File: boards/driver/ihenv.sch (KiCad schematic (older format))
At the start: 8 parts, among them Q63 MMBT2222, Q64 MMBT2907, Q65 MMBT2222

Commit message: Driver board: a bit more schematic work and some initial footprint selections
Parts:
- R175, R176, R177, R178, R179: footprint Resistor_SMD:R_1206_3216Metric -> Resistor_SMD:R_0603_1608Metric
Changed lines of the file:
@@
 F 0 "R170" V 3745 3650 50  0000 C CNN
 F 1 "1k" V 3836 3650 50  0000 C CNN
-F 2 "Resistor_SMD:R_1206_3216Metric" V 3990 3640 50  0001 C CNN
+F 2 "Resistor_SMD:R_0603_1608Metric" V 3990 3640 50  0001 C CNN
 F 3 "~" H 3950 3650 50  0001 C CNN
 	1    3950 3650
@@
 F 0 "R172" H 4568 3296 50  0000 L CNN
 F 1 "2k" H 4568 3205 50  0000 L CNN
-F 2 "Resistor_SMD:R_1206_3216Metric" V 4540 3240 50  0001 C CNN
+F 2 "Resistor_SMD:R_0603_1608Metric" V 4540 3240 50  0001 C CNN
 F 3 "~" H 4500 3250 50  0001 C CNN
 	1    4500 3250
@@
 F 0 "R171" H 4568 2896 50  0000 L CNN
 F 1 "470" H 4568 2805 50  0000 L CNN
-F 2 "Resistor_SMD:R_1206_3216Metric" V 4540 2840 50  0001 C CNN
+F 2 "Resistor_SMD:R_0603_1608Metric" V 4540 2840 50  0001 C CNN
 F 3 "~" H 4500 2850 50  0001 C CNN
 	1    4500 2850
@@
 F 0 "R173" H 5168 3746 50  0000 L CNN
 F 1 "750" H 5168 3655 50  0000 L CNN
-F 2 "Resistor_SMD:R_1206_3216Metric" V 5140 3690 50  0001 C CNN
+F 2 "Resistor_SMD:R_0603_1608Metric" V 5140 3690 50  0001 C CNN
 F 3 "~" H 5100 3700 50  0001 C CNN
 	1    5100 3700
@@
 F 0 "R174" H 5718 3946 50  0000 L CNN
 F 1 "2k" H 5718 3855 50  0000 L CNN
-F 2 "Resistor_SMD:R_1206_3216Metric" V 5690 3890 50  0001 C CNN
+F 2 "Resistor_SMD:R_0603_1608Metric" V 5690 3890 50  0001 C CNN
 F 3 "~" H 5650 3900 50  0001 C CNN
 	1    5650 3900

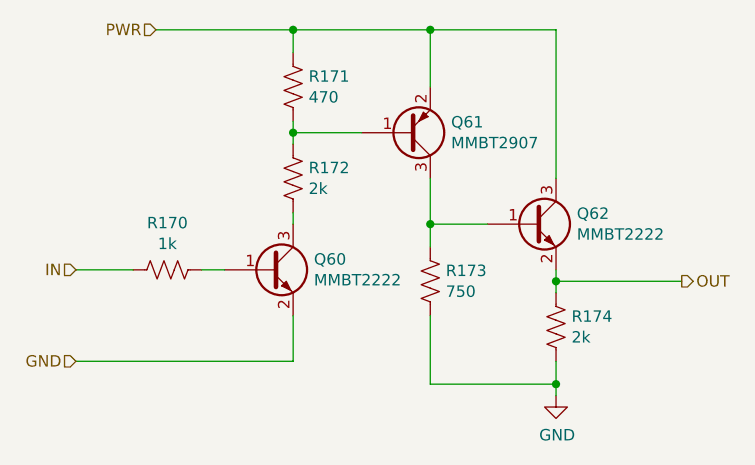
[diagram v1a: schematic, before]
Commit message: Driver board: finished first rough draft schematic. Lots of placeholders, but at least every place is held.
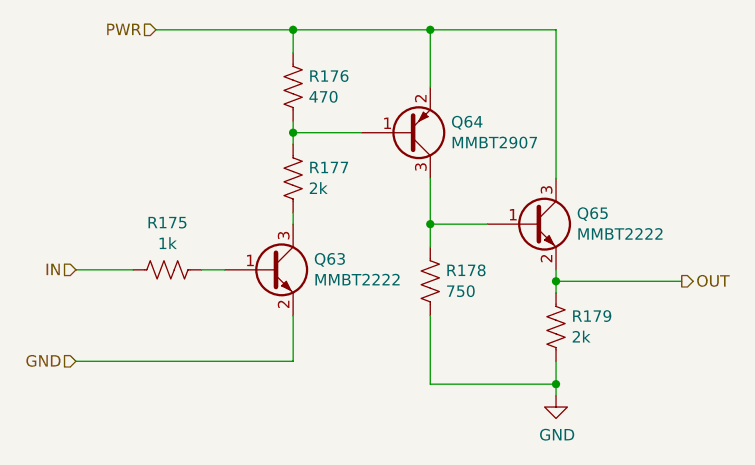
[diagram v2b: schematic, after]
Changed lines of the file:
@@
 $Descr A4 11693 8268
 encoding utf-8
-Sheet 48 68
+Sheet 48 69
 Title ""
 Date ""
@@
 AR Path="/6183FAE6/62401C49/62406F41" Ref="R175"  Part="1"
 AR Path="/6183FAE6/62435917/62406F41" Ref="R170"  Part="1"
-F 0 "R170" V 3745 3650 50  0000 C CNN
+F 0 "R175" V 3745 3650 50  0000 C CNN
 F 1 "1k" V 3836 3650 50  0000 C CNN
 F 2 "Resistor_SMD:R_0603_1608Metric" V 3990 3640 50  0001 C CNN
@@
 AR Path="/6183FAE6/62401C49/62406F48" Ref="Q63"  Part="1"
 AR Path="/6183FAE6/62435917/62406F48" Ref="Q60"  Part="1"
-F 0 "Q60" H 4591 3696 50  0000 L CNN
+F 0 "Q63" H 4591 3696 50  0000 L CNN
 F 1 "MMBT2222" H 4591 3605 50  0000 L CNN
 F 2 "Package_TO_SOT_SMD:SOT-23" H 4600 3750 50  0001 C CNN
@@
 AR Path="/6183FAE6/62401C49/62406F7D" Ref="Q64"  Part="1"
 AR Path="/6183FAE6/62435917/62406F7D" Ref="Q61"  Part="1"
-F 0 "Q61" H 5191 3004 50  0000 L CNN
+F 0 "Q64" H 5191 3004 50  0000 L CNN
 F 1 "MMBT2907" H 5191 3095 50  0000 L CNN
 F 2 "Package_TO_SOT_SMD:SOT-23" H 5200 3150 50  0001 C CNN
@@
 AR Path="/6183FAE6/62401C49/62413636" Ref="R177"  Part="1"
 AR Path="/6183FAE6/62435917/62413636" Ref="R172"  Part="1"
-F 0 "R172" H 4568 3296 50  0000 L CNN
+F 0 "R177" H 4568 3296 50  0000 L CNN
 F 1 "2k" H 4568 3205 50  0000 L CNN
 F 2 "Resistor_SMD:R_0603_1608Metric" V 4540 3240 50  0001 C CNN
@@
 AR Path="/6183FAE6/62401C49/6241520E" Ref="R176"  Part="1"
 AR Path="/6183FAE6/62435917/6241520E" Ref="R171"  Part="1"
-F 0 "R171" H 4568 2896 50  0000 L CNN
+F 0 "R176" H 4568 2896 50  0000 L CNN
 F 1 "470" H 4568 2805 50  0000 L CNN
 F 2 "Resistor_SMD:R_0603_1608Metric" V 4540 2840 50  0001 C CNN
@@
 AR Path="/6183FAE6/62401C49/6241645F" Ref="Q65"  Part="1"
 AR Path="/6183FAE6/62435917/6241645F" Ref="Q62"  Part="1"
-F 0 "Q62" H 5741 3496 50  0000 L CNN
+F 0 "Q65" H 5741 3496 50  0000 L CNN
 F 1 "MMBT2222" H 5741 3405 50  0000 L CNN
 F 2 "Package_TO_SOT_SMD:SOT-23" H 5750 3550 50  0001 C CNN
@@
 AR Path="/6183FAE6/62401C49/624171F4" Ref="R178"  Part="1"
 AR Path="/6183FAE6/62435917/624171F4" Ref="R173"  Part="1"
-F 0 "R173" H 5168 3746 50  0000 L CNN
+F 0 "R178" H 5168 3746 50  0000 L CNN
 F 1 "750" H 5168 3655 50  0000 L CNN
 F 2 "Resistor_SMD:R_0603_1608Metric" V 5140 3690 50  0001 C CNN
@@
 AR Path="/6183FAE6/62401C49/62417AC4" Ref="R179"  Part="1"
 AR Path="/6183FAE6/62435917/62417AC4" Ref="R174"  Part="1"
-F 0 "R174" H 5718 3946 50  0000 L CNN
+F 0 "R179" H 5718 3946 50  0000 L CNN
 F 1 "2k" H 5718 3855 50  0000 L CNN
 F 2 "Resistor_SMD:R_0603_1608Metric" V 5690 3890 50  0001 C CNN

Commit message: Driver board: fleshed out the hotswap controller, tweaked some resistors, and added some bypass caps
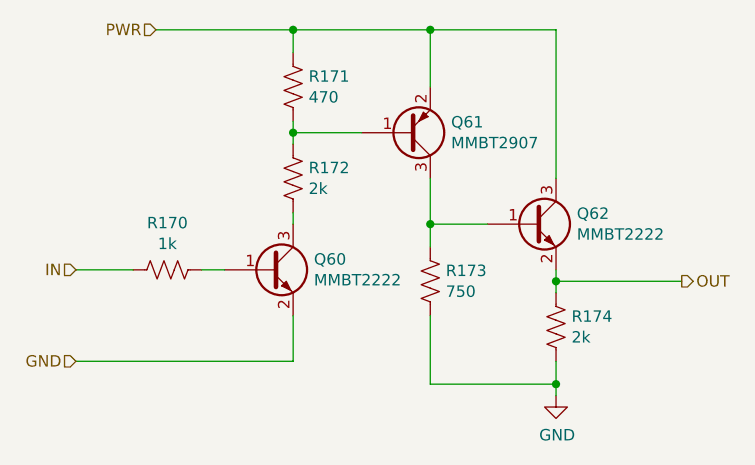
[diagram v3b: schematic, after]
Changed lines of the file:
@@
 AR Path="/6183FAE6/62401C49/62406F41" Ref="R175"  Part="1"
 AR Path="/6183FAE6/62435917/62406F41" Ref="R170"  Part="1"
-F 0 "R175" V 3745 3650 50  0000 C CNN
+F 0 "R170" V 3745 3650 50  0000 C CNN
 F 1 "1k" V 3836 3650 50  0000 C CNN
 F 2 "Resistor_SMD:R_0603_1608Metric" V 3990 3640 50  0001 C CNN
@@
 AR Path="/6183FAE6/62401C49/62406F48" Ref="Q63"  Part="1"
 AR Path="/6183FAE6/62435917/62406F48" Ref="Q60"  Part="1"
-F 0 "Q63" H 4591 3696 50  0000 L CNN
+F 0 "Q60" H 4591 3696 50  0000 L CNN
 F 1 "MMBT2222" H 4591 3605 50  0000 L CNN
 F 2 "Package_TO_SOT_SMD:SOT-23" H 4600 3750 50  0001 C CNN
@@
 AR Path="/6183FAE6/623E7DB1/62406FBD" Ref="#PWR?"  Part="1"
 AR Path="/6183FAE6/623E7DC0/62406FBD" Ref="#PWR?"  Part="1"
-AR Path="/6183FAE6/62401C49/62406FBD" Ref="#PWR079"  Part="1"
-AR Path="/6183FAE6/62435917/62406FBD" Ref="#PWR078"  Part="1"
-F 0 "#PWR079" H 5650 3950 50  0001 C CNN
+AR Path="/6183FAE6/62401C49/62406FBD" Ref="#PWR082"  Part="1"
+AR Path="/6183FAE6/62435917/62406FBD" Ref="#PWR081"  Part="1"
+F 0 "#PWR081" H 5650 3950 50  0001 C CNN
 F 1 "GND" H 5655 4027 50  0000 C CNN
 F 2 "" H 5650 4200 50  0001 C CNN
@@
 AR Path="/6183FAE6/62401C49/62406F7D" Ref="Q64"  Part="1"
 AR Path="/6183FAE6/62435917/62406F7D" Ref="Q61"  Part="1"
-F 0 "Q64" H 5191 3004 50  0000 L CNN
+F 0 "Q61" H 5191 3004 50  0000 L CNN
 F 1 "MMBT2907" H 5191 3095 50  0000 L CNN
 F 2 "Package_TO_SOT_SMD:SOT-23" H 5200 3150 50  0001 C CNN
@@
 AR Path="/6183FAE6/62401C49/62413636" Ref="R177"  Part="1"
 AR Path="/6183FAE6/62435917/62413636" Ref="R172"  Part="1"
-F 0 "R177" H 4568 3296 50  0000 L CNN
+F 0 "R172" H 4568 3296 50  0000 L CNN
 F 1 "2k" H 4568 3205 50  0000 L CNN
 F 2 "Resistor_SMD:R_0603_1608Metric" V 4540 3240 50  0001 C CNN
@@
 AR Path="/6183FAE6/62401C49/6241520E" Ref="R176"  Part="1"
 AR Path="/6183FAE6/62435917/6241520E" Ref="R171"  Part="1"
-F 0 "R176" H 4568 2896 50  0000 L CNN
+F 0 "R171" H 4568 2896 50  0000 L CNN
 F 1 "470" H 4568 2805 50  0000 L CNN
 F 2 "Resistor_SMD:R_0603_1608Metric" V 4540 2840 50  0001 C CNN
@@
 AR Path="/6183FAE6/62401C49/6241645F" Ref="Q65"  Part="1"
 AR Path="/6183FAE6/62435917/6241645F" Ref="Q62"  Part="1"
-F 0 "Q65" H 5741 3496 50  0000 L CNN
+F 0 "Q62" H 5741 3496 50  0000 L CNN
 F 1 "MMBT2222" H 5741 3405 50  0000 L CNN
 F 2 "Package_TO_SOT_SMD:SOT-23" H 5750 3550 50  0001 C CNN
@@
 AR Path="/6183FAE6/62401C49/624171F4" Ref="R178"  Part="1"
 AR Path="/6183FAE6/62435917/624171F4" Ref="R173"  Part="1"
-F 0 "R178" H 5168 3746 50  0000 L CNN
+F 0 "R173" H 5168 3746 50  0000 L CNN
 F 1 "750" H 5168 3655 50  0000 L CNN
 F 2 "Resistor_SMD:R_0603_1608Metric" V 5140 3690 50  0001 C CNN
@@
 AR Path="/6183FAE6/62401C49/62417AC4" Ref="R179"  Part="1"
 AR Path="/6183FAE6/62435917/62417AC4" Ref="R174"  Part="1"
-F 0 "R179" H 5718 3946 50  0000 L CNN
+F 0 "R174" H 5718 3946 50  0000 L CNN
 F 1 "2k" H 5718 3855 50  0000 L CNN
 F 2 "Resistor_SMD:R_0603_1608Metric" V 5690 3890 50  0001 C CNN

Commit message: Driver board: significant cleanup. Moved sense amp pairs into a subsheet, split tuning resistors into two globally, pushed input circuits into their corresponding sheets.
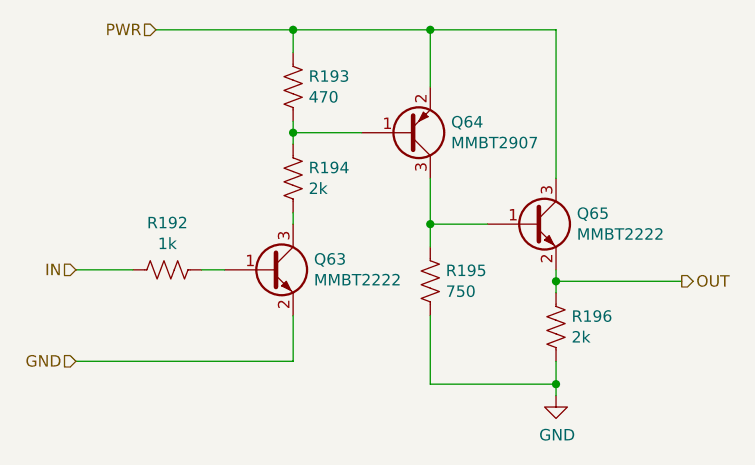
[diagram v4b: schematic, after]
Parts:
- renumbered R175 to R192, R176 to R193, R177 to R194, R178 to R195, R179 to R196
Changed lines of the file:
@@
 $Descr A4 11693 8268
 encoding utf-8
-Sheet 48 69
+Sheet 48 64
 Title ""
 Date ""
@@
 AR Path="/6183FAE6/623E7DB1/62406F41" Ref="R?"  Part="1"
 AR Path="/6183FAE6/623E7DC0/62406F41" Ref="R?"  Part="1"
-AR Path="/6183FAE6/62401C49/62406F41" Ref="R175"  Part="1"
-AR Path="/6183FAE6/62435917/62406F41" Ref="R170"  Part="1"
-F 0 "R170" V 3745 3650 50  0000 C CNN
+AR Path="/6183FAE6/62401C49/62406F41" Ref="R192"  Part="1"
+AR Path="/6183FAE6/62435917/62406F41" Ref="R187"  Part="1"
+F 0 "R192" V 3745 3650 50  0000 C CNN
 F 1 "1k" V 3836 3650 50  0000 C CNN
 F 2 "Resistor_SMD:R_0603_1608Metric" V 3990 3640 50  0001 C CNN
@@
 AR Path="/6183FAE6/62401C49/62406F48" Ref="Q63"  Part="1"
 AR Path="/6183FAE6/62435917/62406F48" Ref="Q60"  Part="1"
-F 0 "Q60" H 4591 3696 50  0000 L CNN
+F 0 "Q63" H 4591 3696 50  0000 L CNN
 F 1 "MMBT2222" H 4591 3605 50  0000 L CNN
 F 2 "Package_TO_SOT_SMD:SOT-23" H 4600 3750 50  0001 C CNN
@@
 AR Path="/6183FAE6/623E7DB1/62406FBD" Ref="#PWR?"  Part="1"
 AR Path="/6183FAE6/623E7DC0/62406FBD" Ref="#PWR?"  Part="1"
-AR Path="/6183FAE6/62401C49/62406FBD" Ref="#PWR082"  Part="1"
-AR Path="/6183FAE6/62435917/62406FBD" Ref="#PWR081"  Part="1"
-F 0 "#PWR081" H 5650 3950 50  0001 C CNN
+AR Path="/6183FAE6/62401C49/62406FBD" Ref="#PWR099"  Part="1"
+AR Path="/6183FAE6/62435917/62406FBD" Ref="#PWR098"  Part="1"
+F 0 "#PWR099" H 5650 3950 50  0001 C CNN
 F 1 "GND" H 5655 4027 50  0000 C CNN
 F 2 "" H 5650 4200 50  0001 C CNN
@@
 AR Path="/6183FAE6/62401C49/62406F7D" Ref="Q64"  Part="1"
 AR Path="/6183FAE6/62435917/62406F7D" Ref="Q61"  Part="1"
-F 0 "Q61" H 5191 3004 50  0000 L CNN
+F 0 "Q64" H 5191 3004 50  0000 L CNN
 F 1 "MMBT2907" H 5191 3095 50  0000 L CNN
 F 2 "Package_TO_SOT_SMD:SOT-23" H 5200 3150 50  0001 C CNN
@@
 OUT
 $Comp
-L Device:R_US R177
+L Device:R_US R194
 U 1 1 62413636
 P 4500 3250
-AR Path="/6183FAE6/62401C49/62413636" Ref="R177"  Part="1"
-AR Path="/6183FAE6/62435917/62413636" Ref="R172"  Part="1"
-F 0 "R172" H 4568 3296 50  0000 L CNN
+AR Path="/6183FAE6/62401C49/62413636" Ref="R194"  Part="1"
+AR Path="/6183FAE6/62435917/62413636" Ref="R189"  Part="1"
+F 0 "R194" H 4568 3296 50  0000 L CNN
 F 1 "2k" H 4568 3205 50  0000 L CNN
 F 2 "Resistor_SMD:R_0603_1608Metric" V 4540 3240 50  0001 C CNN
@@
 	4500 3400 4500 3450
 $Comp
-L Device:R_US R176
+L Device:R_US R193
 U 1 1 6241520E
 P 4500 2850
-AR Path="/6183FAE6/62401C49/6241520E" Ref="R176"  Part="1"
-AR Path="/6183FAE6/62435917/6241520E" Ref="R171"  Part="1"
-F 0 "R171" H 4568 2896 50  0000 L CNN
+AR Path="/6183FAE6/62401C49/6241520E" Ref="R193"  Part="1"
+AR Path="/6183FAE6/62435917/6241520E" Ref="R188"  Part="1"
+F 0 "R193" H 4568 2896 50  0000 L CNN
 F 1 "470" H 4568 2805 50  0000 L CNN
 F 2 "Resistor_SMD:R_0603_1608Metric" V 4540 2840 50  0001 C CNN
@@
 AR Path="/6183FAE6/62401C49/6241645F" Ref="Q65"  Part="1"
 AR Path="/6183FAE6/62435917/6241645F" Ref="Q62"  Part="1"
-F 0 "Q62" H 5741 3496 50  0000 L CNN
+F 0 "Q65" H 5741 3496 50  0000 L CNN
 F 1 "MMBT2222" H 5741 3405 50  0000 L CNN
 F 2 "Package_TO_SOT_SMD:SOT-23" H 5750 3550 50  0001 C CNN
@@
 	5100 3450 5350 3450
 $Comp
-L Device:R_US R178
+L Device:R_US R195
 U 1 1 624171F4
 P 5100 3700
-AR Path="/6183FAE6/62401C49/624171F4" Ref="R178"  Part="1"
-AR Path="/6183FAE6/62435917/624171F4" Ref="R173"  Part="1"
-F 0 "R173" H 5168 3746 50  0000 L CNN
+AR Path="/6183FAE6/62401C49/624171F4" Ref="R195"  Part="1"
+AR Path="/6183FAE6/62435917/624171F4" Ref="R190"  Part="1"
+F 0 "R195" H 5168 3746 50  0000 L CNN
 F 1 "750" H 5168 3655 50  0000 L CNN
 F 2 "Resistor_SMD:R_0603_1608Metric" V 5140 3690 50  0001 C CNN
@@
 Connection ~ 5100 3450
 $Comp
-L Device:R_US R179
+L Device:R_US R196
 U 1 1 62417AC4
 P 5650 3900
-AR Path="/6183FAE6/62401C49/62417AC4" Ref="R179"  Part="1"
-AR Path="/6183FAE6/62435917/62417AC4" Ref="R174"  Part="1"
-F 0 "R174" H 5718 3946 50  0000 L CNN
+AR Path="/6183FAE6/62401C49/62417AC4" Ref="R196"  Part="1"
+AR Path="/6183FAE6/62435917/62417AC4" Ref="R191"  Part="1"
+F 0 "R196" H 5718 3946 50  0000 L CNN
 F 1 "2k" H 5718 3855 50  0000 L CNN
 F 2 "Resistor_SMD:R_0603_1608Metric" V 5690 3890 50  0001 C CNN

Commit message: Driver board: integrated DIN 41612 backplane connector, and made a dedicated parity inhibit sheet with a different set resistor value.
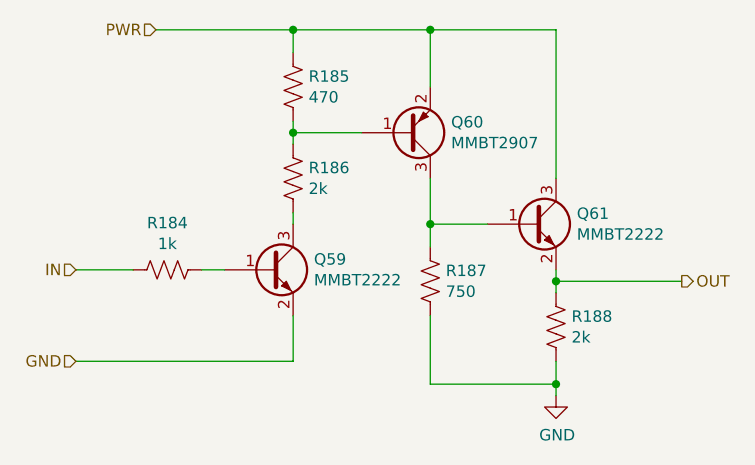
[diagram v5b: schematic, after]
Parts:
- renumbered Q63 to Q59, Q64 to Q60, Q65 to Q61, R192 to R184, R193 to R185, R194 to R186, R195 to R187, R196 to R188
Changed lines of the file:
@@
 AR Path="/6183FAE6/623E7DB1/62406F41" Ref="R?"  Part="1"
 AR Path="/6183FAE6/623E7DC0/62406F41" Ref="R?"  Part="1"
-AR Path="/6183FAE6/62401C49/62406F41" Ref="R192"  Part="1"
-AR Path="/6183FAE6/62435917/62406F41" Ref="R187"  Part="1"
-F 0 "R192" V 3745 3650 50  0000 C CNN
+AR Path="/6183FAE6/62401C49/62406F41" Ref="R184"  Part="1"
+AR Path="/6183FAE6/62435917/62406F41" Ref="R179"  Part="1"
+F 0 "R184" V 3745 3650 50  0000 C CNN
 F 1 "1k" V 3836 3650 50  0000 C CNN
 F 2 "Resistor_SMD:R_0603_1608Metric" V 3990 3640 50  0001 C CNN
@@
 AR Path="/6183FAE6/623E7DB1/62406F48" Ref="Q?"  Part="1"
 AR Path="/6183FAE6/623E7DC0/62406F48" Ref="Q?"  Part="1"
-AR Path="/6183FAE6/62401C49/62406F48" Ref="Q63"  Part="1"
-AR Path="/6183FAE6/62435917/62406F48" Ref="Q60"  Part="1"
-F 0 "Q63" H 4591 3696 50  0000 L CNN
+AR Path="/6183FAE6/62401C49/62406F48" Ref="Q59"  Part="1"
+AR Path="/6183FAE6/62435917/62406F48" Ref="Q56"  Part="1"
+F 0 "Q59" H 4591 3696 50  0000 L CNN
 F 1 "MMBT2222" H 4591 3605 50  0000 L CNN
 F 2 "Package_TO_SOT_SMD:SOT-23" H 4600 3750 50  0001 C CNN
@@
 AR Path="/6183FAE6/623E7DB1/62406FBD" Ref="#PWR?"  Part="1"
 AR Path="/6183FAE6/623E7DC0/62406FBD" Ref="#PWR?"  Part="1"
-AR Path="/6183FAE6/62401C49/62406FBD" Ref="#PWR099"  Part="1"
-AR Path="/6183FAE6/62435917/62406FBD" Ref="#PWR098"  Part="1"
-F 0 "#PWR099" H 5650 3950 50  0001 C CNN
+AR Path="/6183FAE6/62401C49/62406FBD" Ref="#PWR098"  Part="1"
+AR Path="/6183FAE6/62435917/62406FBD" Ref="#PWR097"  Part="1"
+F 0 "#PWR098" H 5650 3950 50  0001 C CNN
 F 1 "GND" H 5655 4027 50  0000 C CNN
 F 2 "" H 5650 4200 50  0001 C CNN
@@
 AR Path="/6183FAE6/623E7DB1/62406F7D" Ref="Q?"  Part="1"
 AR Path="/6183FAE6/623E7DC0/62406F7D" Ref="Q?"  Part="1"
-AR Path="/6183FAE6/62401C49/62406F7D" Ref="Q64"  Part="1"
-AR Path="/6183FAE6/62435917/62406F7D" Ref="Q61"  Part="1"
-F 0 "Q64" H 5191 3004 50  0000 L CNN
+AR Path="/6183FAE6/62401C49/62406F7D" Ref="Q60"  Part="1"
+AR Path="/6183FAE6/62435917/62406F7D" Ref="Q57"  Part="1"
+F 0 "Q60" H 5191 3004 50  0000 L CNN
 F 1 "MMBT2907" H 5191 3095 50  0000 L CNN
 F 2 "Package_TO_SOT_SMD:SOT-23" H 5200 3150 50  0001 C CNN
@@
 OUT
 $Comp
-L Device:R_US R194
+L Device:R_US R186
 U 1 1 62413636
 P 4500 3250
-AR Path="/6183FAE6/62401C49/62413636" Ref="R194"  Part="1"
-AR Path="/6183FAE6/62435917/62413636" Ref="R189"  Part="1"
-F 0 "R194" H 4568 3296 50  0000 L CNN
+AR Path="/6183FAE6/62401C49/62413636" Ref="R186"  Part="1"
+AR Path="/6183FAE6/62435917/62413636" Ref="R181"  Part="1"
+F 0 "R186" H 4568 3296 50  0000 L CNN
 F 1 "2k" H 4568 3205 50  0000 L CNN
 F 2 "Resistor_SMD:R_0603_1608Metric" V 4540 3240 50  0001 C CNN
@@
 	4500 3400 4500 3450
 $Comp
-L Device:R_US R193
+L Device:R_US R185
 U 1 1 6241520E
 P 4500 2850
-AR Path="/6183FAE6/62401C49/6241520E" Ref="R193"  Part="1"
-AR Path="/6183FAE6/62435917/6241520E" Ref="R188"  Part="1"
-F 0 "R193" H 4568 2896 50  0000 L CNN
+AR Path="/6183FAE6/62401C49/6241520E" Ref="R185"  Part="1"
+AR Path="/6183FAE6/62435917/6241520E" Ref="R180"  Part="1"
+F 0 "R185" H 4568 2896 50  0000 L CNN
 F 1 "470" H 4568 2805 50  0000 L CNN
 F 2 "Resistor_SMD:R_0603_1608Metric" V 4540 2840 50  0001 C CNN
@@
 AR Path="/6183FAE6/623E7DB1/6241645F" Ref="Q?"  Part="1"
 AR Path="/6183FAE6/623E7DC0/6241645F" Ref="Q?"  Part="1"
-AR Path="/6183FAE6/62401C49/6241645F" Ref="Q65"  Part="1"
-AR Path="/6183FAE6/62435917/6241645F" Ref="Q62"  Part="1"
-F 0 "Q65" H 5741 3496 50  0000 L CNN
+AR Path="/6183FAE6/62401C49/6241645F" Ref="Q61"  Part="1"
+AR Path="/6183FAE6/62435917/6241645F" Ref="Q58"  Part="1"
+F 0 "Q61" H 5741 3496 50  0000 L CNN
 F 1 "MMBT2222" H 5741 3405 50  0000 L CNN
 F 2 "Package_TO_SOT_SMD:SOT-23" H 5750 3550 50  0001 C CNN
@@
 	5100 3450 5350 3450
 $Comp
-L Device:R_US R195
+L Device:R_US R187
 U 1 1 624171F4
 P 5100 3700
-AR Path="/6183FAE6/62401C49/624171F4" Ref="R195"  Part="1"
-AR Path="/6183FAE6/62435917/624171F4" Ref="R190"  Part="1"
-F 0 "R195" H 5168 3746 50  0000 L CNN
+AR Path="/6183FAE6/62401C49/624171F4" Ref="R187"  Part="1"
+AR Path="/6183FAE6/62435917/624171F4" Ref="R182"  Part="1"
+F 0 "R187" H 5168 3746 50  0000 L CNN
 F 1 "750" H 5168 3655 50  0000 L CNN
 F 2 "Resistor_SMD:R_0603_1608Metric" V 5140 3690 50  0001 C CNN
@@
 Connection ~ 5100 3450
 $Comp
-L Device:R_US R196
+L Device:R_US R188
 U 1 1 62417AC4
 P 5650 3900
-AR Path="/6183FAE6/62401C49/62417AC4" Ref="R196"  Part="1"
-AR Path="/6183FAE6/62435917/62417AC4" Ref="R191"  Part="1"
-F 0 "R196" H 5718 3946 50  0000 L CNN
+AR Path="/6183FAE6/62401C49/62417AC4" Ref="R188"  Part="1"
+AR Path="/6183FAE6/62435917/62417AC4" Ref="R183"  Part="1"
+F 0 "R188" H 5718 3946 50  0000 L CNN
 F 1 "2k" H 5718 3855 50  0000 L CNN
 F 2 "Resistor_SMD:R_0603_1608Metric" V 5690 3890 50  0001 C CNN

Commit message: Driver board: largely fleshed out part selection
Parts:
- Q59, Q61: Digikey (none) -> https://www.digikey.com/en/products/detail/MMBT2222A-G/641-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; Part Number (none) -> MMBT2222A-G
- Q60: Digikey (none) -> https://www.digikey.com/en/products/detail/MMBT2907A-G/641-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; Part Number (none) -> MMBT2907A-G
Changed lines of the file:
@@
 $Descr A4 11693 8268
 encoding utf-8
-Sheet 48 64
+Sheet 42 64
 Title ""
 Date ""
@@
 F 2 "Package_TO_SOT_SMD:SOT-23" H 4600 3750 50  0001 C CNN
 F 3 "~" H 4400 3650 50  0001 C CNN
+F 4 "https://www.digikey.com/en/products/detail/MMBT2222A-G/641-1942-1-ND/9477875" H 4400 3650 50  0001 C CNN "Digikey"
+F 5 "MMBT2222A-G" H 4400 3650 50  0001 C CNN "Part Number"
 	1    4400 3650
 	1    0    0    -1
@@
 F 2 "Package_TO_SOT_SMD:SOT-23" H 5200 3150 50  0001 C CNN
 F 3 "~" H 5000 3050 50  0001 C CNN
+F 4 "https://www.digikey.com/en/products/detail/MMBT2907A-G/641-1952-1-ND/9477883" H 5000 3050 50  0001 C CNN "Digikey"
+F 5 "MMBT2907A-G" H 5000 3050 50  0001 C CNN "Part Number"
 	1    5000 3050
 	1    0    0    1
@@
 F 2 "Package_TO_SOT_SMD:SOT-23" H 5750 3550 50  0001 C CNN
 F 3 "~" H 5550 3450 50  0001 C CNN
+F 4 "https://www.digikey.com/en/products/detail/MMBT2222A-G/641-1942-1-ND/9477875" H 5550 3450 50  0001 C CNN "Digikey"
+F 5 "MMBT2222A-G" H 5550 3450 50  0001 C CNN "Part Number"
 	1    5550 3450
 	1    0    0    -1
